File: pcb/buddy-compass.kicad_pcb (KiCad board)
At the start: 2 copper layers, 64 parts, among them J1 USB_C_Receptacle_USB2.0, J2 Conn_01x02, Q1 DMG2301L, U1 MCP73831-2-OT, U2 LSM303C, U3 W25Q32JVSS, U4 MIC5504-3.3YM5, U5 IS31FL3236A

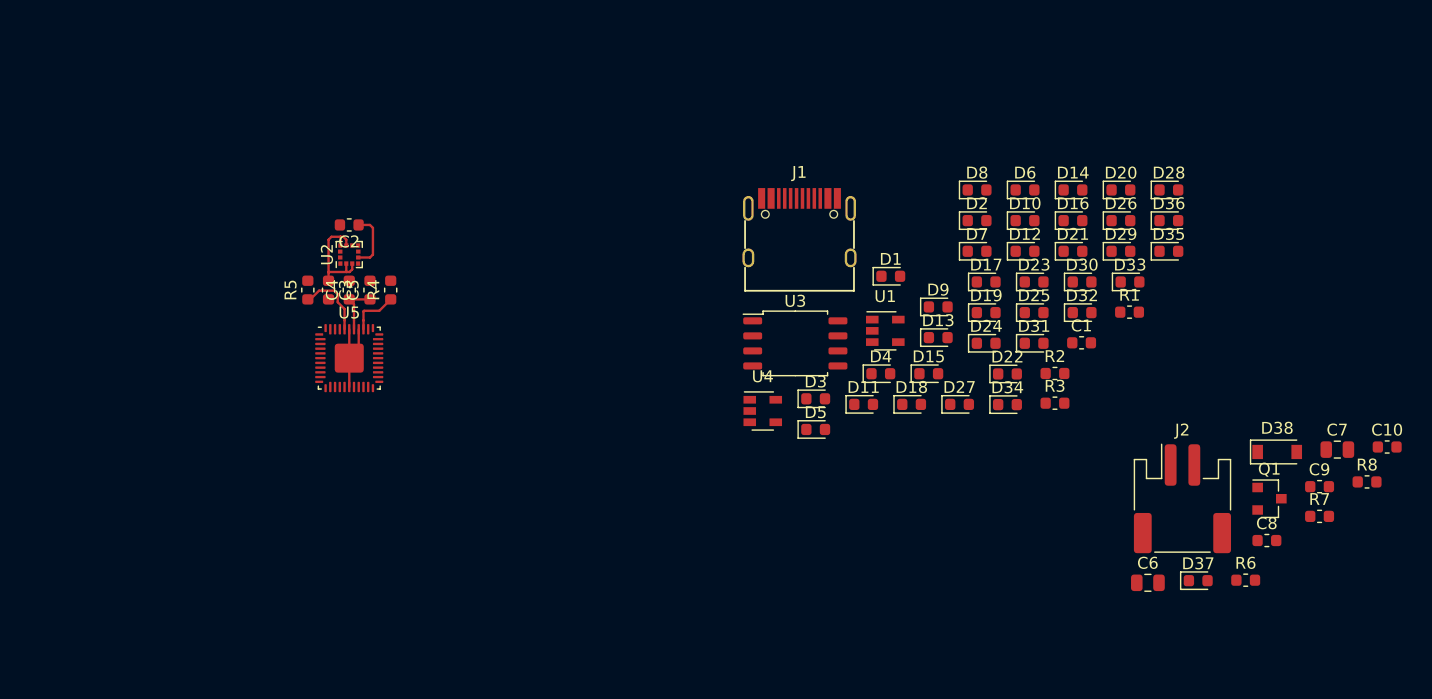
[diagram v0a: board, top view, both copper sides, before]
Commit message: Updating schematic and PCB with LEDs laid out in a circle
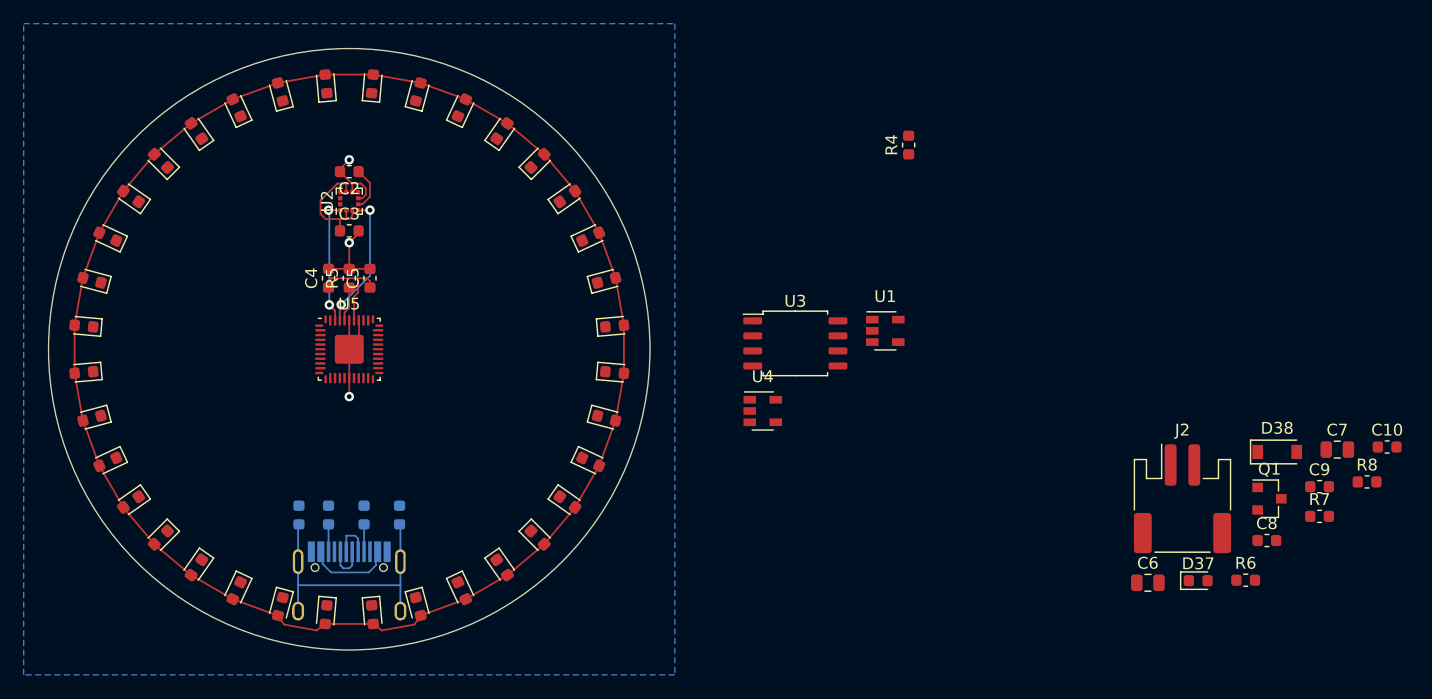
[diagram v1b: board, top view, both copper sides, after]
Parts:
- C1, J1, R1, R2, R3: moved to B.Cu
- moved D28 92.4 mm to (27.6, 48.0), turned to 175 degrees
- moved D26 88.5 mm to (28.3, 55.8), turned to 195 degrees
- moved D29 86.9 mm to (28.3, 44.2), turned to 165 degrees
- moved D30 82.4 mm to (29.6, 40.5), turned to 155 degrees
- moved D33 79.9 mm to (37.1, 31.6), turned to 125 degrees
- moved D25 79.2 mm to (29.6, 59.5), turned to 205 degrees
- moved D20 79.2 mm to (44.2, 71.7), turned to 255 degrees
- moved D32 78.9 mm to (34.1, 34.1), turned to 135 degrees
- moved D31 77.3 mm to (31.6, 37.1), turned to 145 degrees
- moved D23 76.9 mm to (34.1, 65.9), turned to 225 degrees
- moved D35 76.2 mm to (44.2, 28.3), turned to 105 degrees
- moved D21 76.2 mm to (40.5, 70.4), turned to 245 degrees
- moved D27 74.0 mm to (27.6, 52.0), turned to 185 degrees
- moved D24 73.5 mm to (31.6, 62.9), turned to 215 degrees
- moved R1 72.2 mm to (45.8, 64.0), turned to 90 degrees
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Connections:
- U5 pad 1: Net-(D19-Pad1) -> Net-(D34-Pad1)
- U5 pad 10: Net-(D30-Pad1) -> Net-(D25-Pad1)
- U5 pad 11: Net-(D4-Pad1) -> Net-(D24-Pad1)
- U5 pad 12: Net-(D13-Pad1) -> Net-(D23-Pad1)
- U5 pad 14: Net-(D31-Pad1) -> Net-(D21-Pad1)
- U5 pad 15: Net-(D5-Pad1) -> Net-(D20-Pad1)
- U5 pad 16: Net-(D14-Pad1) -> Net-(D19-Pad1)
- U5 pad 18: Net-(D23-Pad1) -> Net-(D18-Pad1)
- U5 pad 19: Net-(D32-Pad1) -> Net-(D17-Pad1)
- U5 pad 2: Net-(D28-Pad1) -> Net-(D33-Pad1)
- U5 pad 20: Net-(D6-Pad1) -> Net-(D16-Pad1)
- U5 pad 22: Net-(D24-Pad1) -> Net-(D14-Pad1)
- U5 pad 23: Net-(D33-Pad1) -> Net-(D13-Pad1)
- U5 pad 24: Net-(D7-Pad1) -> Net-(D12-Pad1)
- U5 pad 25: Net-(D16-Pad1) -> Net-(D11-Pad1)
- U5 pad 26: Net-(D25-Pad1) -> Net-(D10-Pad1)
- U5 pad 27: Net-(D34-Pad1) -> Net-(D9-Pad1)
- U5 pad 29: Net-(D17-Pad1) -> Net-(D7-Pad1)
- U5 pad 3: Net-(D2-Pad1) -> Net-(D32-Pad1)
- U5 pad 30: Net-(D26-Pad1) -> Net-(D6-Pad1)
- U5 pad 31: Net-(D35-Pad1) -> Net-(D5-Pad1)
- U5 pad 32: Net-(D9-Pad1) -> Net-(D4-Pad1)
- U5 pad 33: Net-(D18-Pad1) -> Net-(D3-Pad1)
- U5 pad 34: Net-(D27-Pad1) -> Net-(D2-Pad1)
- U5 pad 35: Net-(D36-Pad1) -> Net-(D1-Pad1)
- U5 pad 4: Net-(D11-Pad1) -> Net-(D31-Pad1)
- U5 pad 43: Net-(D1-Pad1) -> Net-(D36-Pad1)
- U5 pad 44: Net-(D10-Pad1) -> Net-(D35-Pad1)
- U5 pad 5: Net-(D20-Pad1) -> Net-(D30-Pad1)
- U5 pad 7: Net-(D3-Pad1) -> Net-(D28-Pad1)
- U5 pad 8: Net-(D12-Pad1) -> Net-(D27-Pad1)
- U5 pad 9: Net-(D21-Pad1) -> Net-(D26-Pad1)
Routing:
- net VCC: track 4.44 -> 155.8 mm
- net Net-(C1-Pad1): track 0.00 -> 23.4 mm
- net GND: track 7.64 -> 25.4 mm, vias 0 -> 3
- net /SDA: track 0.00 -> 11.4 mm, vias 0 -> 2
- net /SCL: track 0.00 -> 10.5 mm, vias 0 -> 2
- net VBUS: track 0.00 -> 7.82 mm
- net Net-(R4-Pad1): track 4.23 -> 0.00 mm
- net /D-: track 0.00 -> 3.55 mm
- net /D+: track 0.00 -> 3.51 mm
- net Net-(R5-Pad1): track 6.15 -> 2.94 mm
- net Net-(J1-PadB5): track 0.00 -> 2.31 mm
- net Net-(J1-PadA5): track 0.00 -> 2.31 mm
- net Net-(C2-Pad1): track 4.91 -> 3.77 mm
- net +3V3: track 9.71 -> 10.6 mm
- added copper zone on B.Cu, net GND
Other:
- board outline added: 50.8 x 50.8 mm

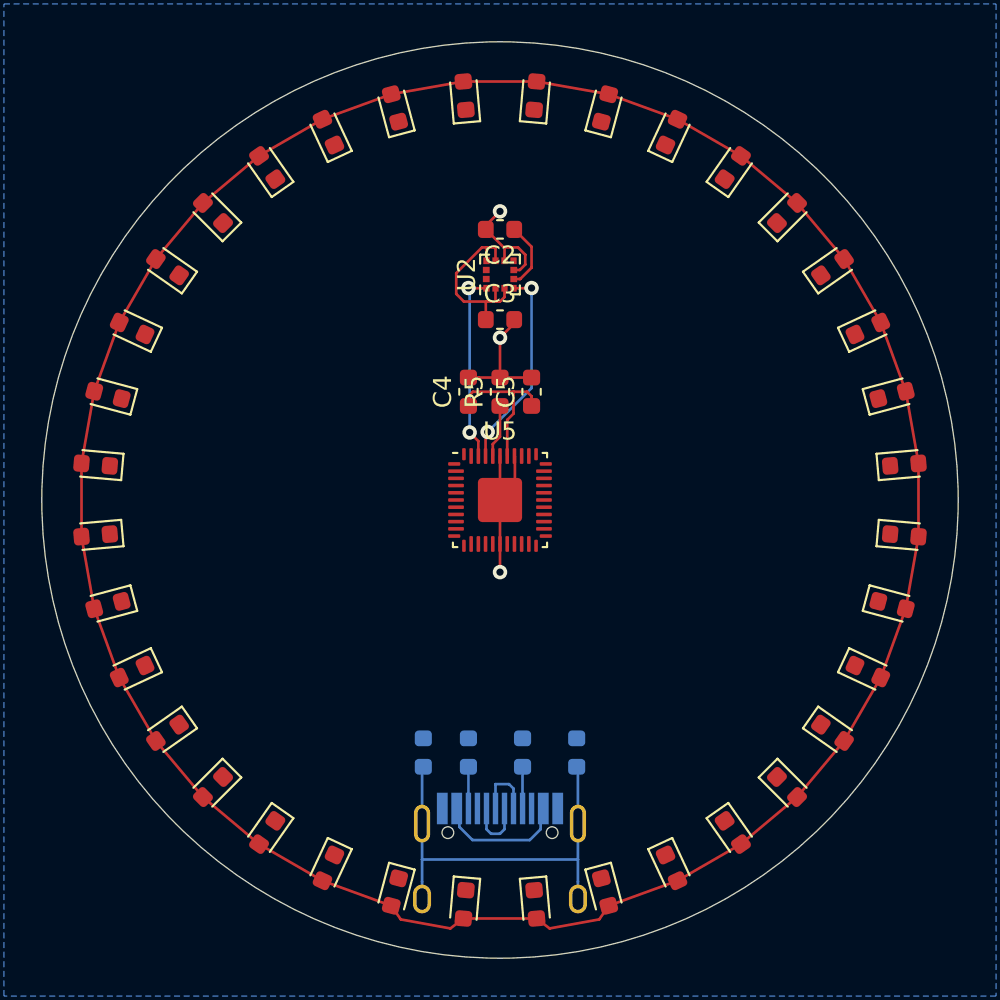
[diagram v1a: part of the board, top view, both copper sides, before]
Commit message: Making some progress on the top layout. Need to rework around the compass.
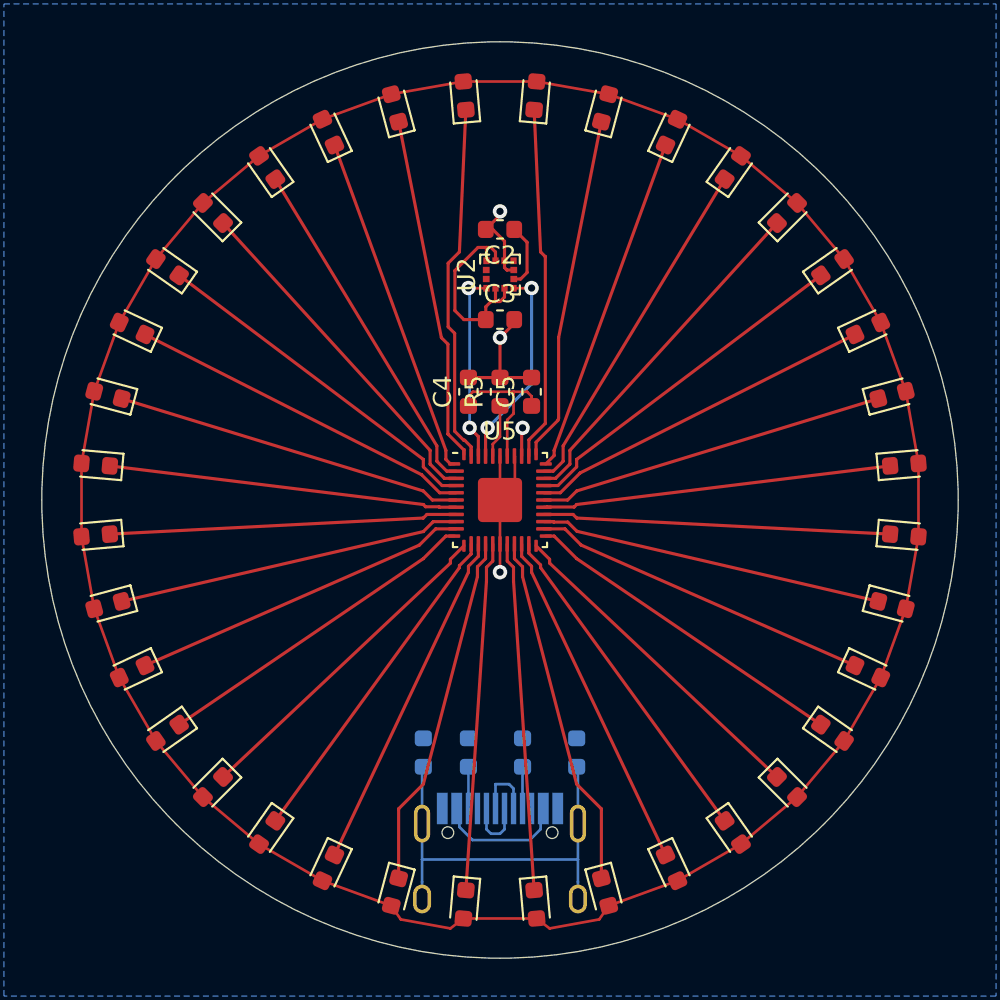
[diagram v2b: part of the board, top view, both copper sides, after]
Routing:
- net Net-(D36-Pad1): track 0.00 -> 20.0 mm
- net Net-(D1-Pad1): track 0.00 -> 19.7 mm
- net Net-(D20-Pad1): track 0.00 -> 19.7 mm
- net Net-(D17-Pad1): track 0.00 -> 19.7 mm
- net Net-(D31-Pad1): track 0.00 -> 19.6 mm
- net Net-(D6-Pad1): track 0.00 -> 19.6 mm
- net Net-(D32-Pad1): track 0.00 -> 19.6 mm
- net Net-(D5-Pad1): track 0.00 -> 19.6 mm
- net Net-(D7-Pad1): track 0.00 -> 19.5 mm
- net Net-(D30-Pad1): track 0.00 -> 19.5 mm
- net Net-(D29-Pad1): track 0.00 -> 19.5 mm
- net Net-(D8-Pad1): track 0.00 -> 19.5 mm
- net Net-(D33-Pad1): track 0.00 -> 19.4 mm
- net Net-(D4-Pad1): track 0.00 -> 19.4 mm
- net Net-(D28-Pad1): track 0.00 -> 19.4 mm
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
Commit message: Added buttons and footprint for MCU module. Layout for buttons and power supply is done. Still need to tweak sensor layout and LED driver layout to fit MCU underneath.
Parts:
- added C11: 12p, Capacitor_SMD:C_0603_1608Metric, B.Cu at (108.2, 67.0)
- added C12: 12p, Capacitor_SMD:C_0603_1608Metric, B.Cu at (114.2, 67.0)
- added C13: 1u, Capacitor_SMD:C_0603_1608Metric, B.Cu at (106.2, 67.0)
- added C14: 100n, Capacitor_SMD:C_0603_1608Metric, B.Cu at (104.2, 67.0)
- added J3: Conn_ARM_JTAG_SWD_10, Connector_PinHeader_1.27mm:PinHeader_2x05_P1.27mm_Vertical_SMD, B.Cu at (88.2, 52.8)
- added R10: 47K, Resistor_SMD:R_0603_1608Metric, B.Cu at (70.2, 50.0)
- added R11: 47K, Resistor_SMD:R_0603_1608Metric, B.Cu at (67.5, 59.8)
- added R12: 47K, Resistor_SMD:R_0603_1608Metric, B.Cu at (32.5, 40.2)
- added R13: 47K, Resistor_SMD:R_0603_1608Metric, B.Cu at (29.8, 50.0)
- added R14: 47K, Resistor_SMD:R_0603_1608Metric, B.Cu at (32.5, 60.0)
- added R9: 47K, Resistor_SMD:R_0603_1608Metric, B.Cu at (67.5, 40.2)
- added SW1: SW_Push, buddy-compass-parts:TS-1236VW, B.Cu at (70.0, 38.8)
- added SW2: SW_Push, buddy-compass-parts:TS-1236VW, B.Cu at (73.0, 50.0)
- added SW3: SW_Push, buddy-compass-parts:TS-1236VW, B.Cu at (70.0, 61.2)
- added SW4: SW_Push, buddy-compass-parts:TS-1236VW, B.Cu at (30.0, 38.8)
- added SW5: SW_Push, buddy-compass-parts:TS-1236VW, B.Cu at (27.0, 50.0)
- added SW6: SW_Push, buddy-compass-parts:TS-1236VW, B.Cu at (30.0, 61.2)
- added U6: E73-2G4M08S1C, buddy-compass-parts:E73-2G4M08S1C, B.Cu at (107.5, 55.0)
- added Y1: 32.768KHz, Crystal:Crystal_SMD_3215-2Pin_3.2x1.5mm, B.Cu at (111.2, 67.0)
- C10, C6, C7, C8, C9, D37, D38, J2, Q1, R4, R6, R7, R8, U1, U3, U4: moved to B.Cu
- moved R8 98.9 mm to (37.2, 67.8), turned to 90 degrees
- moved C7 98.6 mm to (35.0, 64.0), turned to 270 degrees
- moved C10 96.2 mm to (41.5, 56.0), turned to 90 degrees
- moved C8 93.1 mm to (35.0, 56.0), turned to 90 degrees
- moved R7 90.3 mm to (41.8, 67.8), turned to 270 degrees
- moved Q1 89.5 mm to (38.2, 60.0), turned to 180 degrees
- moved D38 85.6 mm to (42.8, 60.0)
- moved D37 82.2 mm to (39.5, 67.8), turned to 90 degrees
- moved R6 82.1 mm to (43.8, 64.0), turned to 270 degrees
- moved C6 76.2 mm to (41.5, 64.0), turned to 270 degrees
- moved J2 60.4 mm to (60.0, 65.0)
- moved U1 59.1 mm to (38.2, 64.0)
- moved U4 46.7 mm to (38.2, 56.0)
- moved C9 36.3 mm to (95.8, 58.5)
- moved U3 8.70 mm to (95.8, 52.8), turned to 270 degrees
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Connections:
- U3 pad 1: (no net) -> /QSPI_CS
- U3 pad 2: (no net) -> /QSPI_D1
- U3 pad 3: (no net) -> /QSPI_D2
- U3 pad 5: (no net) -> /QSPI_D0
- U3 pad 6: (no net) -> /QSPI_SCK
- U3 pad 7: (no net) -> /QSPI_D3
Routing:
- net Net-(C7-Pad1): track 0.00 -> 44.0 mm
- net VBUS: track 7.82 -> 40.2 mm
- net VCC: track 155.8 -> 176.5 mm, vias 0 -> 1
- net GND: track 24.2 -> 44.3 mm
- net +3V3: track 11.4 -> 25.9 mm
- net /QSPI_CS: track 0.00 -> 11.3 mm
- net /QSPI_D2: track 0.00 -> 8.28 mm
- net /QSPI_SCK: track 0.00 -> 8.17 mm
- net /QSPI_D1: track 0.00 -> 7.42 mm
- net /QSPI_D3: track 0.00 -> 7.26 mm
- net Net-(C11-Pad1): track 0.00 -> 5.60 mm
- net Net-(C12-Pad1): track 0.00 -> 5.56 mm
- net Net-(R7-Pad1): track 0.00 -> 4.11 mm
- net /QSPI_D0: track 0.00 -> 3.55 mm
- net /BUTTON5: track 0.00 -> 2.96 mm
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
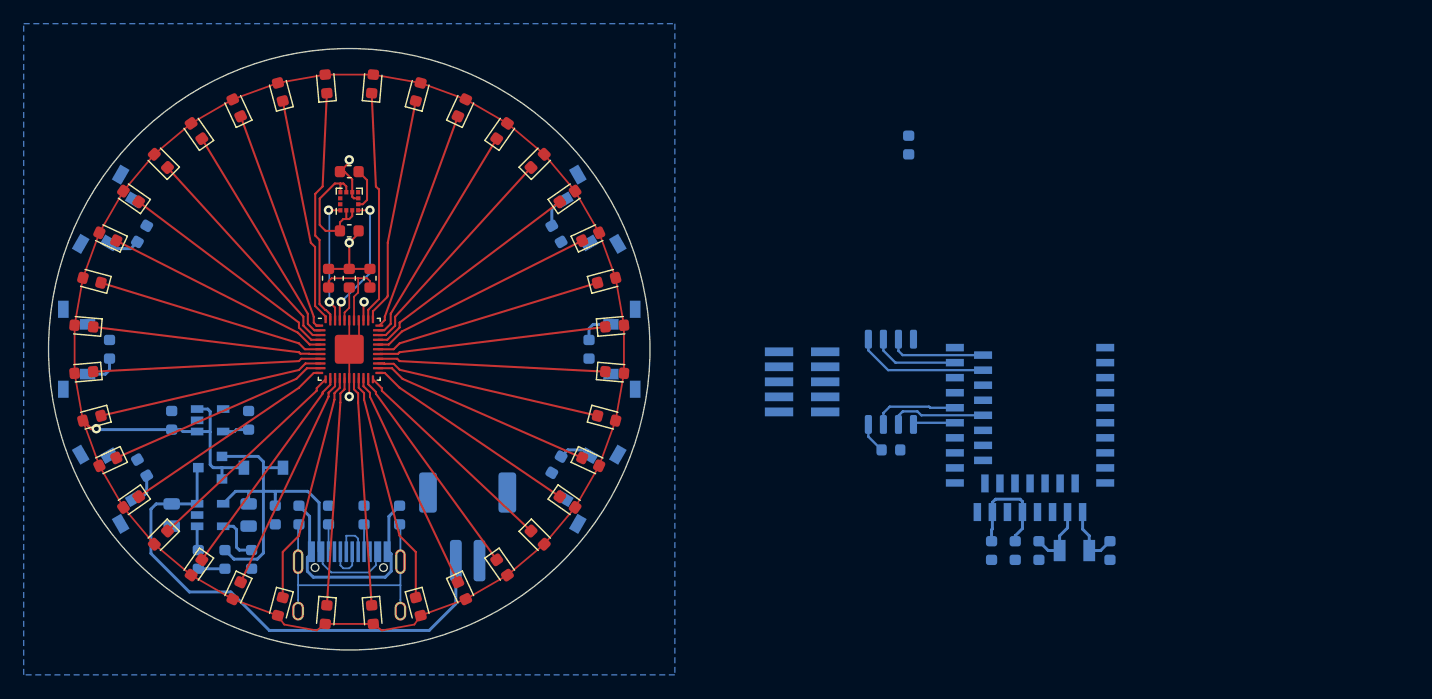
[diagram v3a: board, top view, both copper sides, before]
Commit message: I think I've routed myself into a corner - no way to lay this out properly on 2-layer without adding extraneous stuff to top layer, which would spoil the look.
Moving to a 2-board solution.
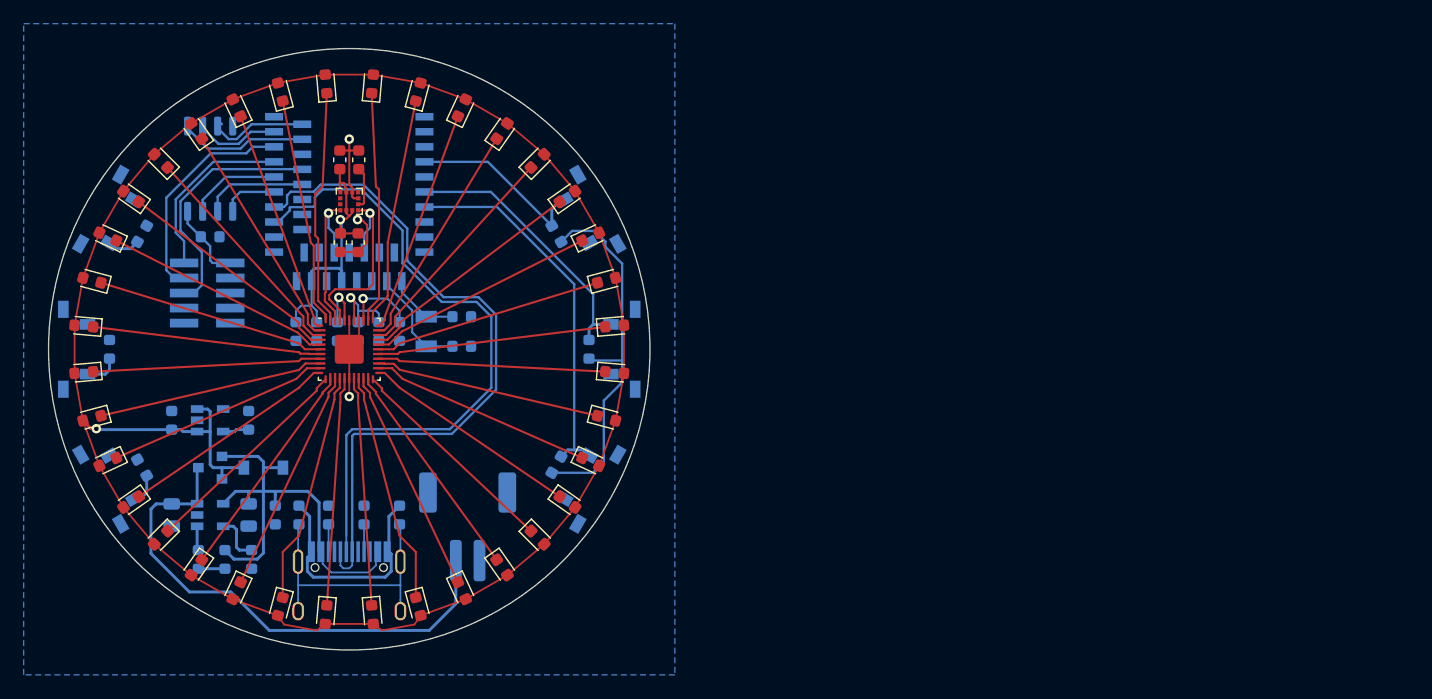
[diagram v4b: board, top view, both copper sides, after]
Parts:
- added C15: 100n, Capacitor_SMD:C_0603_1608Metric, F.Cu at (49.2, 34.0)
- added C16: 1u, Capacitor_SMD:C_0603_1608Metric, F.Cu at (49.2, 41.0)
- C4, C5, R5: moved to B.Cu
- moved C13 61.8 mm to (47.2, 48.5)
- moved C14 61.6 mm to (45.5, 48.5)
- moved U6 60.7 mm to (50.0, 35.5)
- moved C9 60.3 mm to (38.2, 40.5)
- moved U3 60.3 mm to (38.2, 34.8)
- moved C12 58.2 mm to (59.5, 47.2), turned to 0 degrees
- moved Y1 57.8 mm to (56.5, 48.5), turned to 90 degrees
- moved C11 51.7 mm to (59.5, 49.8), turned to 0 degrees
- moved J3 50.8 mm to (38.0, 45.2), turned to 180 degrees
- moved R4 45.8 mm to (54.2, 48.5)
- moved C4 5.15 mm to (50.8, 48.5), turned to 270 degrees
- moved R5 4.61 mm to (49.0, 48.5), turned to 270 degrees
- moved C5 4.56 mm to (52.5, 48.5), turned to 270 degrees
- moved C2 1.28 mm to (50.8, 34.0), turned to 90 degrees
- moved C3 1.25 mm to (50.8, 41.0), turned to 270 degrees
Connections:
- U6 pad 15: /SCL -> (no net)
- U6 pad 16: (no net) -> /SDA
- U6 pad 18: /SDA -> (no net)
- U6 pad 20: (no net) -> /SCL
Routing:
- net /D+: track 3.51 -> 59.5 mm
- net /D-: track 3.55 -> 55.9 mm
- net +3V3: track 25.9 -> 66.1 mm, vias 0 -> 1
- net /BUTTON3: track 2.81 -> 32.2 mm
- net /SWO: track 0.00 -> 21.0 mm
- net /BUTTON2: track 2.96 -> 23.3 mm
- net /SWC: track 0.00 -> 18.8 mm
- net /SWD: track 0.00 -> 15.3 mm
- net /BUTTON1: track 2.80 -> 15.8 mm
- net /SDA: track 11.4 -> 17.6 mm, vias 2 -> 1
- net Net-(R4-Pad1): track 1.58 -> 6.34 mm
- net /SCL: track 10.8 -> 14.6 mm, vias 2 -> 1
- net Net-(C11-Pad1): track 5.60 -> 9.09 mm
- net VCC: track 176.5 -> 174.9 mm, vias 1 -> 2
- net Net-(R5-Pad1): track 2.94 -> 4.29 mm, vias 0 -> 1
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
